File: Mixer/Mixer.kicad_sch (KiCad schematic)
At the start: 32 parts, among them J1 Conn_02x05_Odd_Even, J2 AudioJack2_SwitchT, J3 AudioJack2_SwitchT, J4 AudioJack2_SwitchT, J5 AudioJack2_SwitchT, J6 AudioJack2_SwitchT, J7 AudioJack2_SwitchT, J8 AudioJack2_SwitchT, U1 TL072

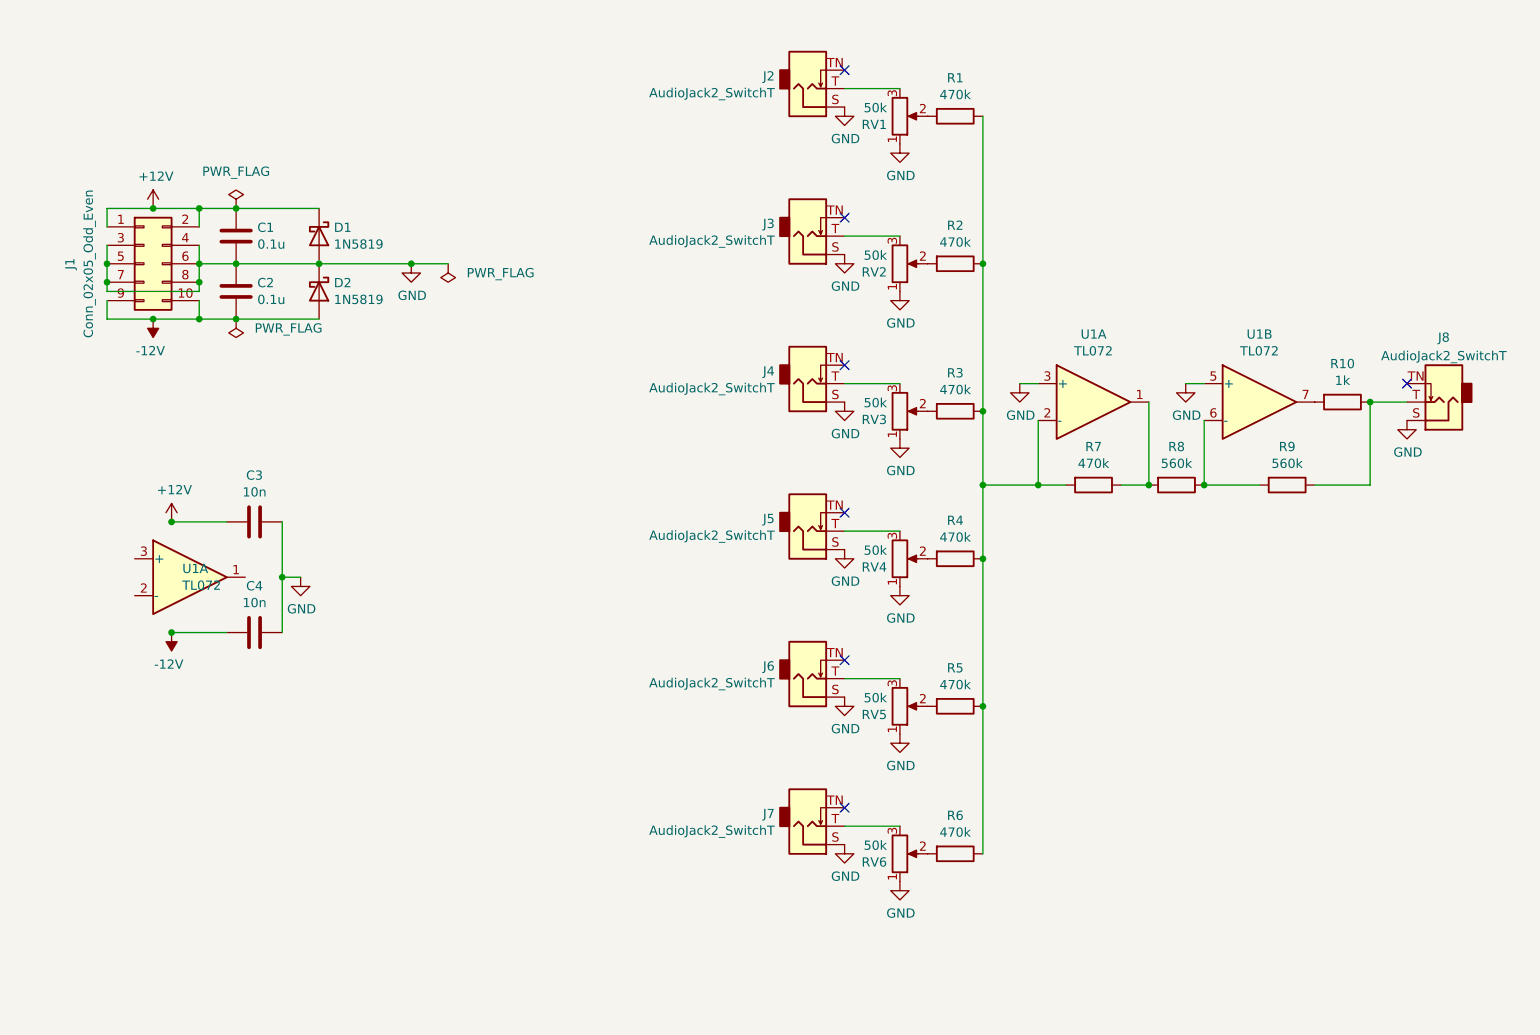
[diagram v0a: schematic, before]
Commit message: Redo mixer schematic
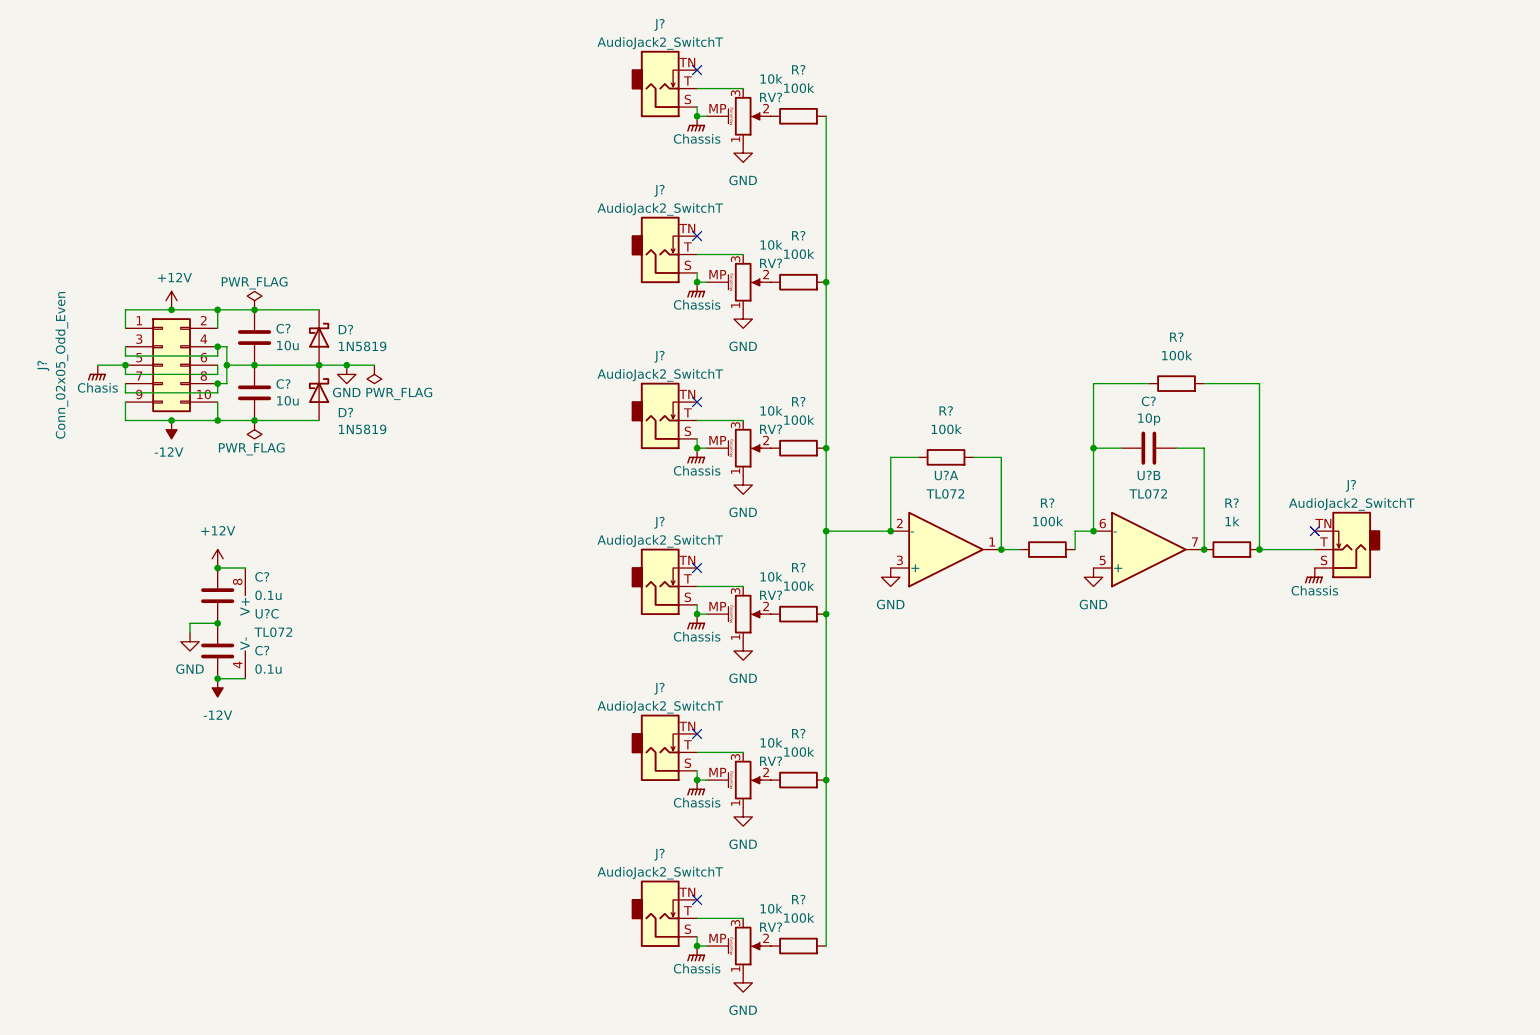
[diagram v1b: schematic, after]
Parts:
- removed C1, C2: 0.1u, Capacitor_THT:C_Disc_D5.0mm_W2.5mm_P5.00mm, symbol Device:C
- removed C3, C4: 10n, Capacitor_THT:C_Disc_D5.0mm_W2.5mm_P5.00mm, symbol Device:C
- removed D1, D2: 1N5819, Diode_THT:D_DO-41_SOD81_P10.16mm_Horizontal, symbol Diode:1N5819
- removed J1: Conn_02x05_Odd_Even, Connector_PinHeader_2.54mm:PinHeader_2x05_P2.54mm_Vertical, symbol Connector_Generic:Conn_02x05_Odd_Even
- removed J2, J3, J4, J5, J6, J7, J8: AudioJack2_SwitchT, Connector_Audio:Jack_3.5mm_QingPu_WQP-PJ398SM_Vertical_CircularHoles, symbol Connector:AudioJack2_SwitchT
- removed R1, R2, R3, R4, R5, R6, R7: 470k, Resistor_THT:R_Axial_DIN0207_L6.3mm_D2.5mm_P7.62mm_Horizontal, symbol Device:R
- removed R10: 1k, Resistor_THT:R_Axial_DIN0207_L6.3mm_D2.5mm_P7.62mm_Horizontal, symbol Device:R
- removed R8, R9: 560k, Resistor_THT:R_Axial_DIN0207_L6.3mm_D2.5mm_P7.62mm_Horizontal, symbol Device:R
- removed RV1, RV2, RV3, RV4, RV5, RV6: 50k, Potentiometer_THT:Potentiometer_Alpha_RD901F-40-00D_Single_Vertical_CircularHoles, symbol Device:R_Potentiometer
- removed U1 (x2): TL072, Package_DIP:DIP-8_W7.62mm_Socket, symbol Amplifier_Operational:TL072
- added C? (x2): 0.1u, symbol Device:C
- added C? (x2): 10u, Capacitor_THT:C_Disc_D5.0mm_W2.5mm_P5.00mm, symbol Device:C
- added C?: 10p, Capacitor_THT:C_Disc_D5.0mm_W2.5mm_P5.00mm, symbol Device:C
- added D? (x2): 1N5819, Diode_THT:D_DO-41_SOD81_P10.16mm_Horizontal, symbol Diode:1N5819
- added J? (x7): AudioJack2_SwitchT, Connector_Audio:Jack_3.5mm_QingPu_WQP-PJ398SM_Vertical_CircularHoles, symbol Connector:AudioJack2_SwitchT
- added J?: Conn_02x05_Odd_Even, Connector_PinHeader_2.54mm:PinHeader_2x05_P2.54mm_Vertical, symbol Connector_Generic:Conn_02x05_Odd_Even
- added R? (x9): 100k, symbol Device:R
- added R?: 1k, symbol Device:R
- added RV? (x6): 10k, symbol Device:R_Potentiometer_MountingPin
- added U? (x3): TL072, symbol Amplifier_Operational:TL072
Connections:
- net +12V: now also C?.1, C?.2, D?.1 (K), J?.1 (Pin_1), J?.2 (Pin_2), U?.8 (V+)
- net -12V: now also C?.1, C?.2, D?.2 (A), J?.10 (Pin_10), J?.9 (Pin_9), U?.4 (V-)
- net GND: now also C?.1, C?.1, C?.2, C?.2, D?.1 (K), D?.2 (A), J?.3 (Pin_3), J?.4 (Pin_4), J?.7 (Pin_7), J?.8 (Pin_8), RV?.1, RV?.1, RV?.1, RV?.1, RV?.1, RV?.1, U?.3 (+), U?.5 (+)
- new net: J?.T, RV?.3 (x6)
- new net: R?.1, RV?.2 (x6)
- new net: R?.1, R?.2, R?.2, R?.2, R?.2, R?.2, R?.2, U?.2 (-)
- new net: C?.1, R?.1, R?.2, U?.6 (-)
- new net: C?.2, R?.1, U?.7
- new net: R?.1, R?.2, U?.1
- new net: J?.T, R?.2, R?.2
- new net Chasis: J?.5 (Pin_5), J?.6 (Pin_6)
- new net Chassis: J?.S, J?.S, J?.S, J?.S, J?.S, J?.S, J?.S, RV?.MP (MountPin), RV?.MP (MountPin), RV?.MP (MountPin), RV?.MP (MountPin), RV?.MP (MountPin), RV?.MP (MountPin)

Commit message: Fix mixer ERC issues
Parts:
- removed C? (x2): 10u, Capacitor_THT:C_Disc_D5.0mm_W2.5mm_P5.00mm, symbol Device:C
- removed D? (x2): 1N5819, Diode_THT:D_DO-41_SOD81_P10.16mm_Horizontal, symbol Diode:1N5819
- removed J?: Conn_02x05_Odd_Even, Connector_PinHeader_2.54mm:PinHeader_2x05_P2.54mm_Vertical, symbol Connector_Generic:Conn_02x05_Odd_Even
- added C3, C4: 10u, Capacitor_THT:C_Disc_D5.0mm_W2.5mm_P5.00mm, symbol Device:C
- added D1, D2: 1N5819, Diode_THT:D_DO-41_SOD81_P10.16mm_Horizontal, symbol Diode:1N5819
- added J1: Conn_02x05_Odd_Even, Connector_PinHeader_2.54mm:PinHeader_2x05_P2.54mm_Vertical, symbol Connector_Generic:Conn_02x05_Odd_Even
- gave numbers to parts that had none: 27
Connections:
- net +12V: now also C3.1, D1.1 (K), J1.1 (Pin_1), J1.2 (Pin_2)
- net -12V: now also C4.2, D2.2 (A), J1.10 (Pin_10), J1.9 (Pin_9)
- net Chassis: now also J1.5 (Pin_5), J1.6 (Pin_6)
- net GND: now also C3.2, C4.1, D1.2 (A), D2.1 (K), J1.3 (Pin_3), J1.4 (Pin_4), J1.7 (Pin_7), J1.8 (Pin_8)
